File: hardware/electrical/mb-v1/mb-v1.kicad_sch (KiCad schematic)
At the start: 38 parts, among them J1 USB_C_Receptacle, J2 Conn_01x16_Socket, J3 Conn_01x06_Socket, SW1 SW_MEC_5E, SW2 SW_MEC_5E, SW3 SW_MEC_5E, SW4 SW_MEC_5E, U1 PCF8574T, U2 CH340E, U3 ATmega328P-A, Y1 16MHz

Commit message: rewire the lcd module section
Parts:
- removed DS1: WC1602A, Display:WC1602A, symbol Display_Character:WC1602A
- removed J1: USB_C_Receptacle, Connector_USB:USB_C_Receptacle_Amphenol_12401548E4-2A, symbol Connector:USB_C_Receptacle
- removed J?: TYPE-C-31-M-12, TYPE-C-31-M-12:HRO_TYPE-C-31-M-12, symbol TYPE-C-31-M-12:TYPE-C-31-M-12
- added C?: 10uF, Capacitor_SMD:C_0805_2012Metric, symbol Device:C
- added C?: 0.1uF, Capacitor_SMD:C_0603_1608Metric, symbol Device:C
- added J4: TYPE-C-31-M-12, TYPE-C-31-M-12:HRO_TYPE-C-31-M-12, symbol TYPE-C-31-M-12:TYPE-C-31-M-12
- added Q?: MMBT2222A, Package_TO_SOT_SMD:SOT-23, symbol Transistor_BJT:MMBT2222A
- added R?: 1k, symbol Device:R_US
- added R? (x4): 10k, Resistor_SMD:R_0603_1608Metric, symbol Device:R_US
- added RV?: 10k, symbol Device:R_Potentiometer_Trim_US
- J2: value Conn_01x16_Socket -> LCD Display Header
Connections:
- net LCD_LED+ is gone; now on net +5V: J2.15 (Pin_15)
- net LCD_R/W is gone; now on net GND: J2.5 (Pin_5)
- net LCD_VDD is gone; now on net +5V: J2.2 (Pin_2)
- net LCD_VSS is gone; now on net GND: J2.1 (Pin_1)
- net +5V: now also C?.1, C?.2, J4.A4_B9 (VBUS), J4.B4_A9 (VBUS), R?.2, R?.2, R?.2, RV?.1; no longer U1.13 (~{INT})
- net GND: now also U1.5 (P1), C?.1, C?.2, J4.A1_B12 (GND), J4.B1_A12 (GND), J4.S1 (SHIELD), J4.S2 (SHIELD), J4.S3 (SHIELD), J4.S4 (SHIELD), Q?.2 (E), R?.2, RV?.3
- net LCD_DB0: no longer U1.4 (P0)
- net LCD_DB1: no longer U1.5 (P1)
- net LCD_DB2: no longer U1.6 (P2)
- net LCD_DB3: no longer U1.7 (P3)
- net LCD_E: now also U1.6 (P2)
- net LCD_LED-: now also Q?.3 (C)
- net LCD_RS: now also U1.4 (P0)
- net LCD_VO: now also RV?.2
- net SCL: now also R?.1
- net SDA: now also R?.1
- net at U2.1 (UD+): now also J4.A6 (DP1), J4.B6 (DP2)
- net at U2.2 (UD-): now also J4.A7 (DN1), J4.B7 (DN2)
- net at R6.1: now also J4.A5 (CC1)
- net at R5.1: now also J4.B5 (CC2)
- new net: R?.1, U1.7 (P3)
- new net: Q?.1 (B), R?.1, R?.2
- new net: R?.1, U1.13 (~{INT})
- no-connect marks 15 -> 11
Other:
- moved on the sheet: BZ1, C10, C11, C2, C5, C6, C7, C8, C9, J2, J3, R5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

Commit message: update readme. change rules
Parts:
- R7: value 5.1k -> 1k
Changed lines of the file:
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@@
 			)
 		)
-		(property "Value" "5.1k"
+		(property "Value" "1k"
 			(at 149.86 97.79 90)
 			(effects

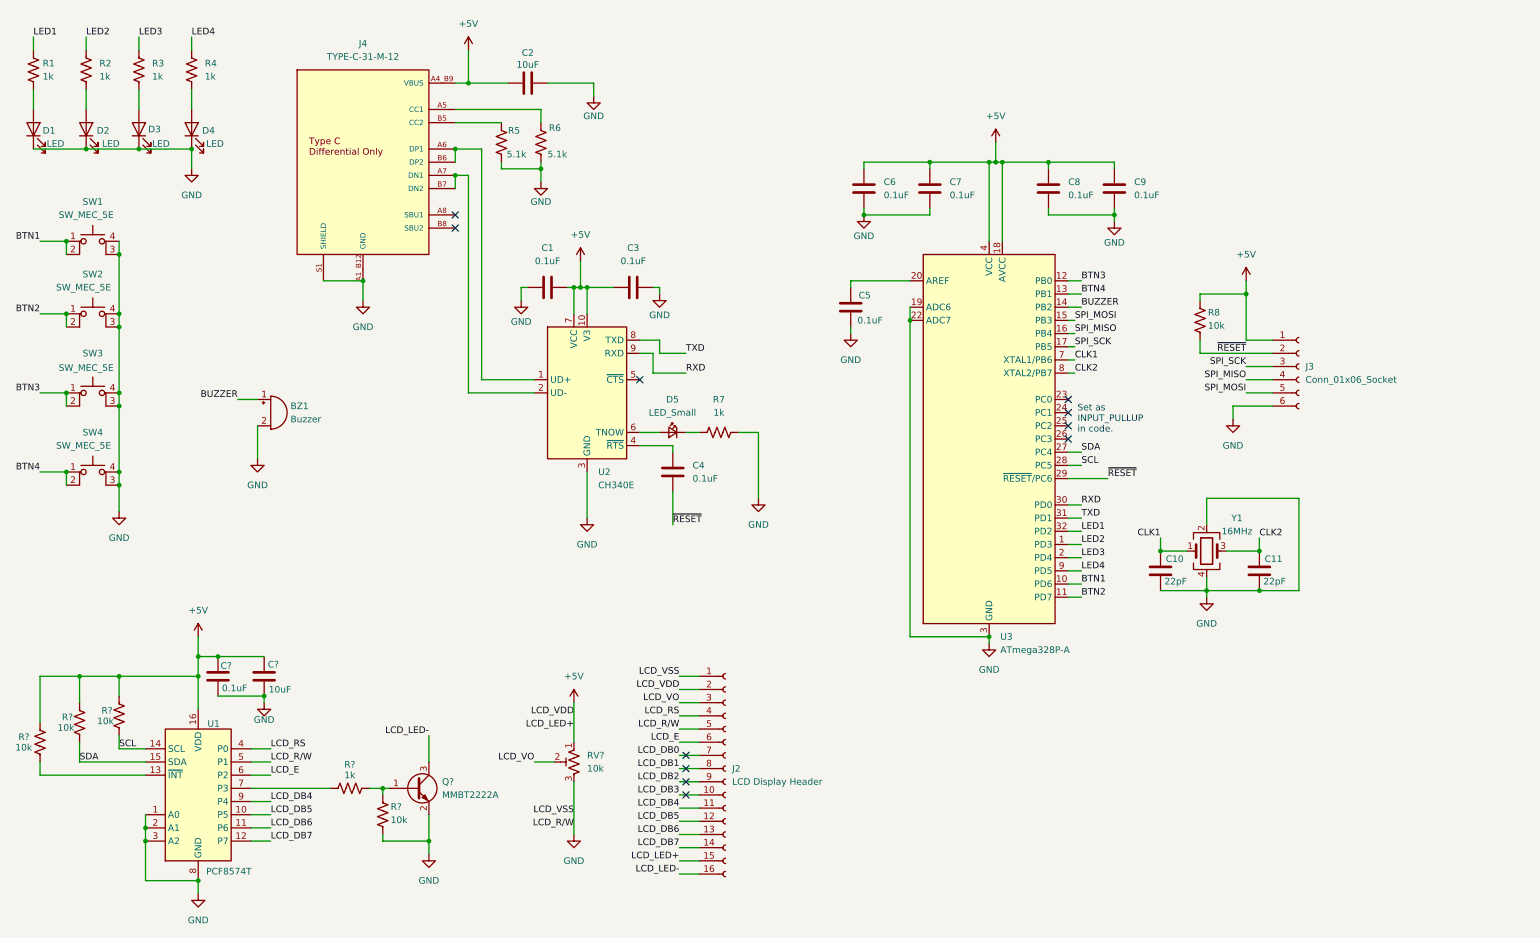
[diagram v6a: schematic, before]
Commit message: assign more footprints
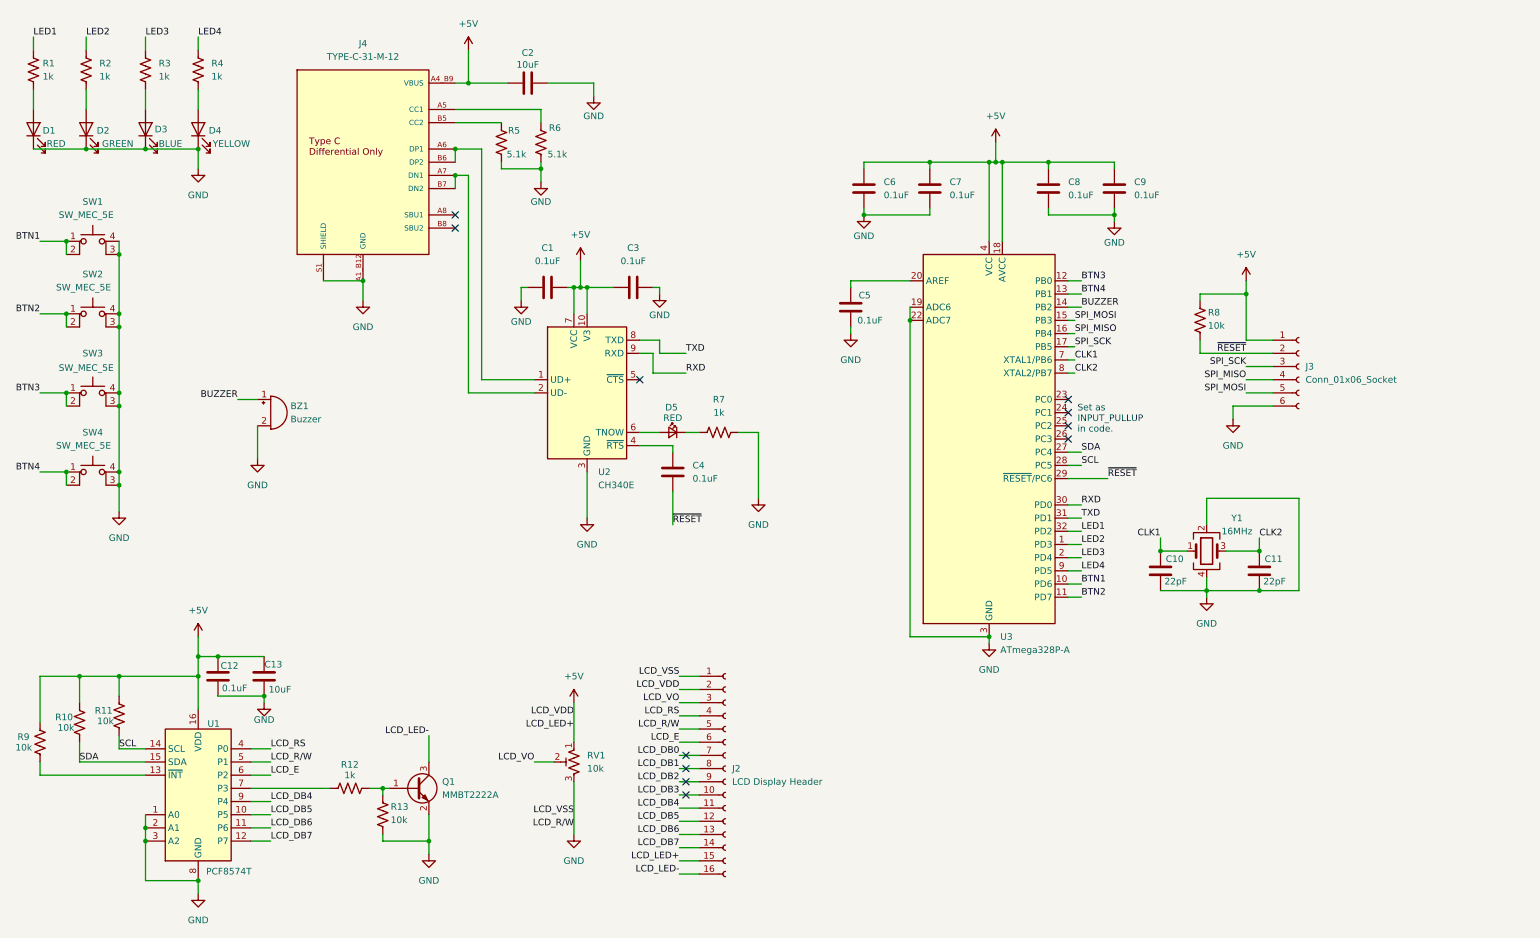
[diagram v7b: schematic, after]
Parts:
- D1: value LED -> RED; footprint (none) -> LED_SMD:LED_0603_1608Metric
- D2: value LED -> GREEN; footprint (none) -> LED_SMD:LED_0603_1608Metric
- D3: value LED -> BLUE; footprint (none) -> LED_SMD:LED_0603_1608Metric
- D4: value LED -> YELLOW; footprint (none) -> LED_SMD:LED_0603_1608Metric
- D5: value LED_Small -> RED; footprint (none) -> LED_SMD:LED_0402_1005Metric
- J2: footprint (none) -> Connector_PinSocket_2.54mm:PinSocket_1x16_P2.54mm_Vertical
- J3: footprint (none) -> Connector_PinSocket_2.54mm:PinSocket_1x06_P2.54mm_Vertical
- gave numbers to parts that had none: 9
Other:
- moved on the sheet: D3, D4, R3, R4
